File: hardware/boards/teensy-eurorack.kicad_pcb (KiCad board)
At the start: 2 copper layers, 118.1 x 224.8 mm, 166 parts, among them J1 Conn_01x08, J10 AudioJack3_SwitchTR, J27 Conn_01x02, J28 Conn_02x08_Odd_Even, J4 AudioJack3_SwitchTR, J5 AudioJack3_SwitchTR, J57 WURTH_ELECTRONICS_61400413321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, J58 USB-A-S-X-X-VT, J6 AudioJack3_SwitchTR, J7 AudioJack3_SwitchTR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

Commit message: silkscreen
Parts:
- U5: value MCP1700-2502E_SOT23 -> MCP1700-2502E
- moved C4 20.0 mm to (206.8, -2.79)
- moved C8 17.9 mm to (214.9, -14.2), turned to 270 degrees
- moved C9 13.6 mm to (212.6, -14.2), turned to 270 degrees
- moved C17 13.5 mm to (219.2, -22.6)
- moved C3 12.6 mm to (215.4, -2.79)
- moved C10 9.31 mm to (210.3, -14.2), turned to 270 degrees
- moved C11 8.86 mm to (217.2, -14.2), turned to 270 degrees
- moved C16 7.90 mm to (219.5, -19.1)
- moved C6 7.60 mm to (209.0, -34.8), turned to 90 degrees
- moved R3 6.02 mm to (195.6, -12.1)
- moved R4 5.50 mm to (195.6, -15.6)
- moved C18 5.35 mm to (208.0, -14.2), turned to 270 degrees
- moved C14 4.49 mm to (205.7, -14.2), turned to 90 degrees
- moved C30 3.99 mm to (184.9, -122.9)
- moved C7 3.32 mm to (206.8, -34.8), turned to 90 degrees
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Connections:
- JB3 pad 2: /ES2 -> /P2
- JB3 pad 3: /ES1 -> /P1
- JB3 pad 4: /P4 -> /E3B
- JB3 pad 5: /P3 -> /E3A
- JB3 pad 6: /P2 -> /ES3
- JB3 pad 7: /P1 -> GND
- JB3 pad 8: GND -> /P3
- JB4 pad 2: /E3B -> /P4
- JB4 pad 3: /E3A -> /ES1
- JB4 pad 4: /E2B -> /E1B
- JB4 pad 5: /E2A -> /E1A
- JB4 pad 6: /E1B -> /ES2
- JB4 pad 7: /E1A -> /E2B
- JB4 pad 8: /ES3 -> /E2A
- JM3 pad 2: /ES2 -> /P2
- JM3 pad 3: /ES1 -> /P1
- JM3 pad 4: /P4 -> /E3B
- JM3 pad 5: /P3 -> /E3A
- JM3 pad 6: /P2 -> /ES3
- JM3 pad 7: /P1 -> GND
- JM3 pad 8: GND -> /P3
- JM4 pad 2: /E3B -> /P4
- JM4 pad 3: /E3A -> /ES1
- JM4 pad 4: /E2B -> /E1B
- JM4 pad 5: /E2A -> /E1A
- JM4 pad 6: /E1B -> /ES2
- JM4 pad 7: /E1A -> /E2B
- JM4 pad 8: /ES3 -> /E2A

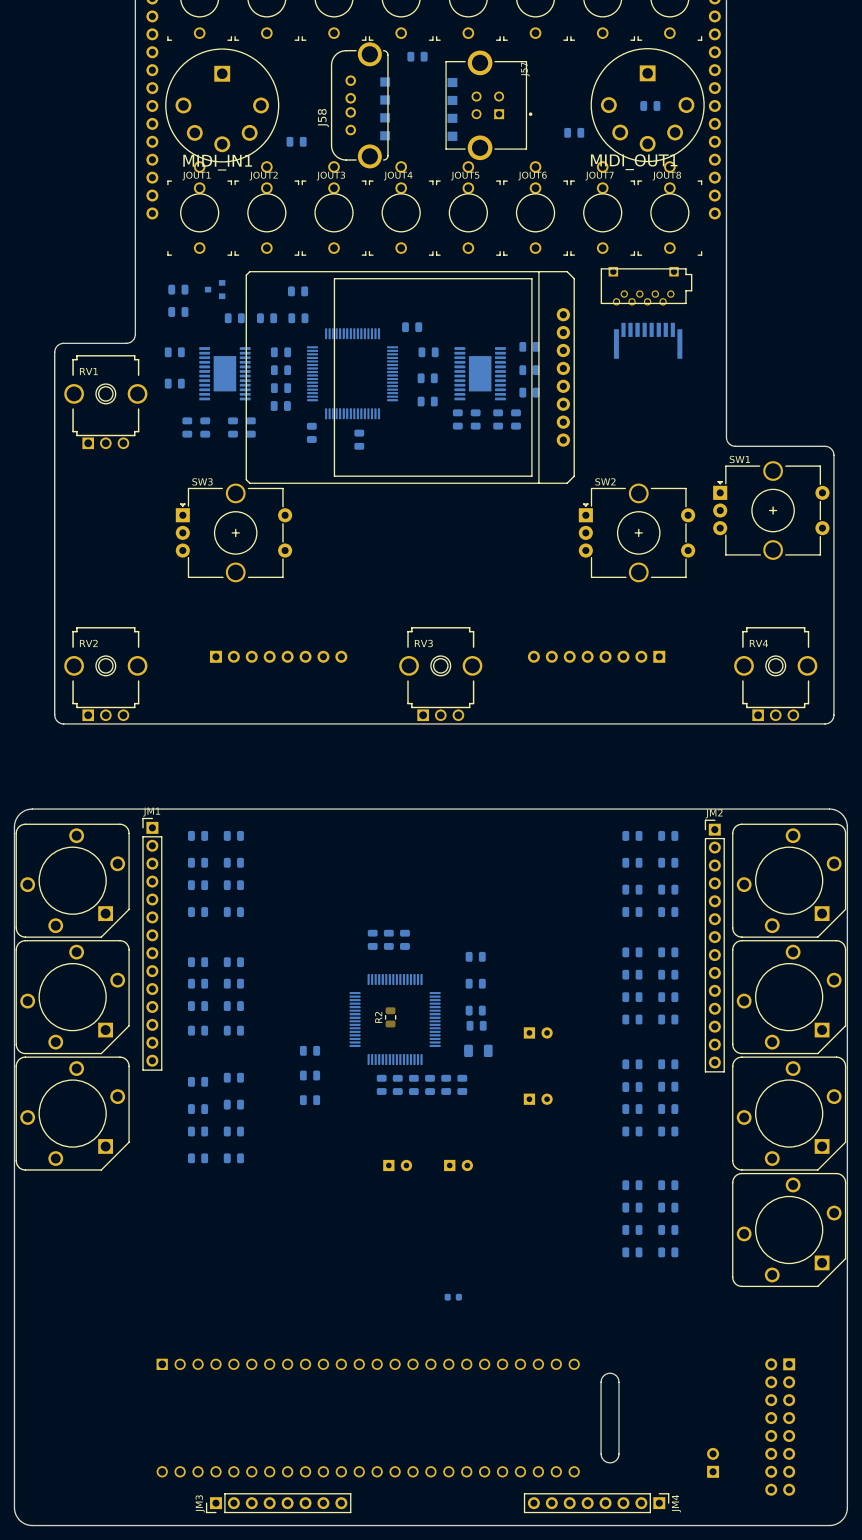
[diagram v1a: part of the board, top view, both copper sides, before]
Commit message: silkscreen, corrections
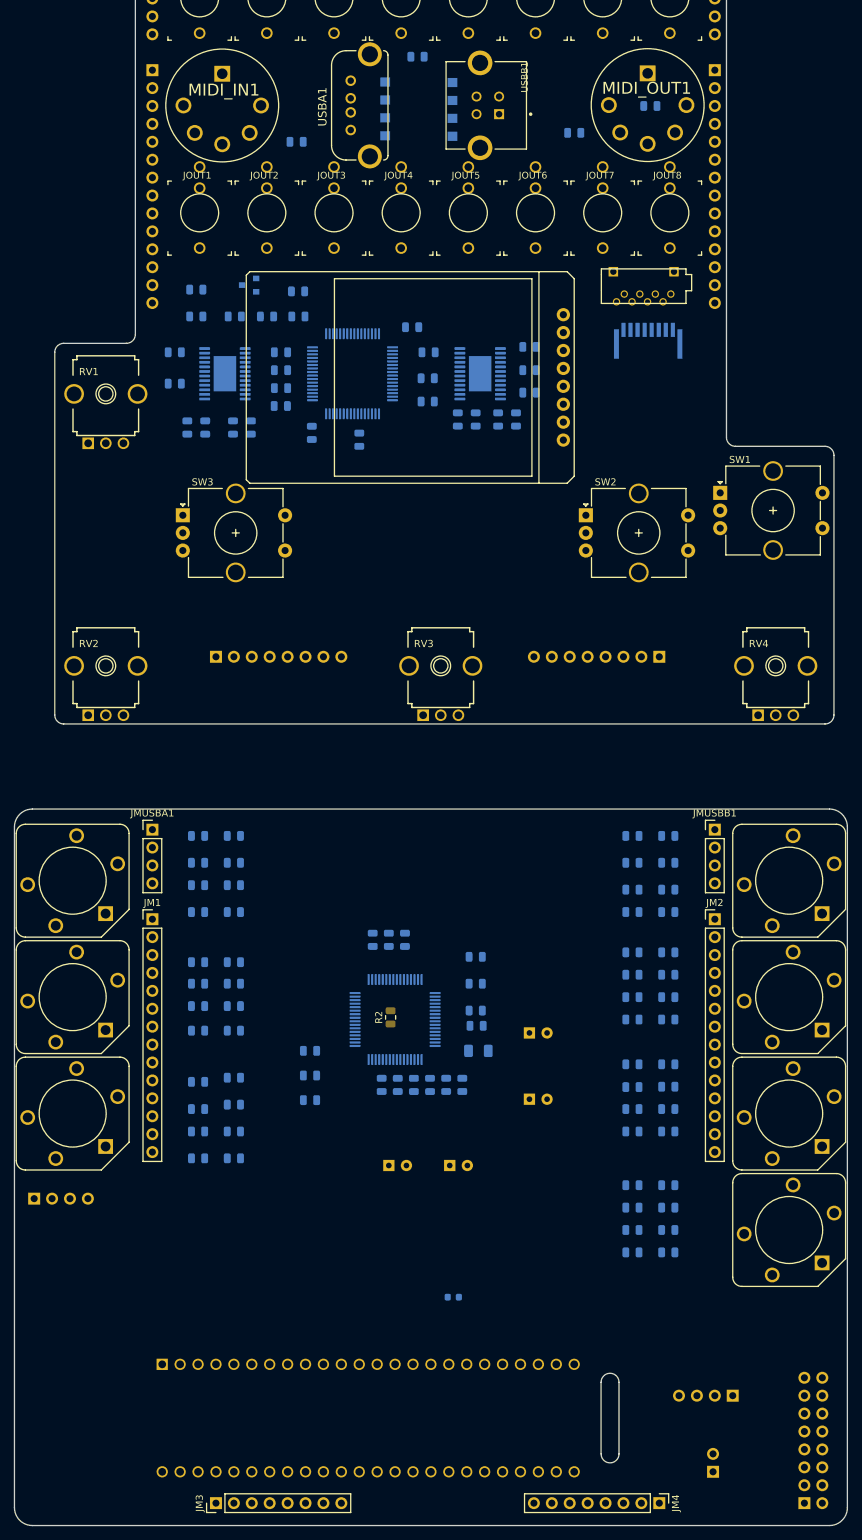
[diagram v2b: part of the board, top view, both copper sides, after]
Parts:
- added JBUSBA1: Conn_01x04, Connector_PinSocket_2.54mm:PinSocket_1x04_P2.54mm_Vertical, B.Cu at (173.2, -170.8)
- added JBUSBB1: Conn_01x04, Connector_PinSocket_2.54mm:PinSocket_1x04_P2.54mm_Vertical, B.Cu at (253.0, -170.8)
- added JMUSBA1: Conn_01x04, Connector_PinHeader_2.54mm:PinHeader_1x04_P2.54mm_Vertical, F.Cu at (173.2, -50.4)
- added JMUSBB1: Conn_01x04, Connector_PinHeader_2.54mm:PinHeader_1x04_P2.54mm_Vertical, F.Cu at (253.0, -50.4)
- added JUSBA1: Conn_01x04, Connector_PinHeader_2.54mm:PinHeader_1x04_P2.54mm_Vertical, B.Cu at (156.5, 1.91)
- added JUSBB1: Conn_01x04, Connector_PinHeader_2.54mm:PinHeader_1x04_P2.54mm_Vertical, B.Cu at (255.5, 29.8)
- C12: value 4.7uF -> 4.7u
- C14: value 22uF -> 22u
- C16: value 100uF -> 100u
- C27, C29, C33, C34, C37: value 10uF -> 10u
- USBB1: renamed from J57; value WURTH_ELECTRONICS_61400413321WURTH_ELECTRONICS_61400413321_0_0 -> 61400413321
- moved J28 19.8 mm to (265.7, 45.1), turned to 0 degrees
- moved JM1 13.0 mm to (173.2, -37.7)
- moved JM2 12.7 mm to (253.0, -37.7)
- moved JB1 12.7 mm to (173.2, -158.1)
- moved JB2 12.7 mm to (253.0, -158.1)
- moved U5 4.87 mm to (186.9, -127.6)
- moved C28 2.62 mm to (179.5, -123.2)
- moved C27 2.54 mm to (179.5, -127.0)
- moved C29 0.25 mm to (189.5, -123.2)
- moved C30 0.25 mm to (184.9, -123.2)
- moved C40 0.25 mm to (193.9, -123.2)
- renumbered J58 to USBA1
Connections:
- USBA1 pad 1: (no net) -> Net-(JBUSBA1-Pad4)
- USBA1 pad 2: (no net) -> Net-(JBUSBA1-Pad3)
- USBA1 pad 3: (no net) -> Net-(JBUSBA1-Pad2)
- USBA1 pad 4: (no net) -> Net-(JBUSBA1-Pad1)
- USBB1 pad 1: (no net) -> Net-(JBUSBB1-Pad4)
- USBB1 pad 2: (no net) -> Net-(JBUSBB1-Pad3)
- USBB1 pad 3: (no net) -> Net-(JBUSBB1-Pad2)
- USBB1 pad 4: (no net) -> GND
- USBB1 pad 5: (no net) -> Net-(USBB1-Pad5)
- USBB1 pad 6: (no net) -> Net-(USBB1-Pad6)

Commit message: split into two boards
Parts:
- removed C19, C20, C21, C22, C27, C29, C33, C34, C37, C42: 10u, Capacitor_SMD:C_0805_2012Metric
- removed C23, C24, C25, C26, C28, C30, C31, C32, C35, C36, C38, C39, C40, C41: 0.1u, Capacitor_SMD:C_0805_2012Metric
- removed C43, C44: 1u, Capacitor_SMD:C_0805_2012Metric
- removed D1: D, Diode_SMD:D_0805_2012Metric
- removed FPC_SD1: 1734592-8, footprints:HFW8R-1STE1LF
- removed J1: Conn_01x08, footprints:ST7735
- removed JB1, JB2: Conn_01x14, Connector_PinSocket_2.54mm:PinSocket_1x14_P2.54mm_Vertical
- removed JB3, JB4: Conn_01x08, Connector_PinSocket_2.54mm:PinSocket_1x08_P2.54mm_Vertical
- removed JBUSBA1, JBUSBB1: Conn_01x04, Connector_PinSocket_2.54mm:PinSocket_1x04_P2.54mm_Vertical
- removed JIN1, JIN2, JIN3, JIN4, JIN5, JIN6, JIN7, JIN8, JOUT1, JOUT2, JOUT3, JOUT4, JOUT5, JOUT6, JOUT7, JOUT8: AudioJack2_SwitchT, footprints:WQP-PJ301M-12_JACK
- removed MIDI_IN1, MIDI_OUT1: DIN-5, footprints:OG-MIDI_SD-50BV
- removed R36, R37, R38: 220, Resistor_SMD:R_0805_2012Metric
- removed R5, R6, R7: 4.7k, Resistor_SMD:R_0805_2012Metric
- removed RV1, RV2, RV3, RV4: R_POT, footprints:9MM_SNAP-IN_POT
- removed SDCARD1: YAMAICHI_SD_CARD, footprints:YAMAICHI_MICROSD_VERTICAL
- removed SW1, SW2, SW3: Rotary_Encoder_Switch, Rotary_Encoder:RotaryEncoder_Alps_EC12E-Switch_Vertical_H20mm_CircularMountingHoles
- removed U2, U3: AD5754BREZ, Package_SO:HTSSOP-24-1EP_4.4x7.8mm_P0.65mm_EP3.2x5mm
- removed U5: MCP1700-2502E, Package_TO_SOT_SMD:SOT-23
- removed U6: AD7606BSTZ, Package_QFP:LQFP-64_10x10mm_P0.5mm
- removed U7: 6N138, footprints:6N138S
- removed USBA1: USB-A-S-X-X-VT, footprints:USB-A-S-X-X-VT
- removed USBB1: 61400413321, footprints:WURTH_ELECTRONICS_61400413321_0
- moved FB1 41.1 mm to (248.7, 40.6)
- moved C15 22.8 mm to (207.1, -13.0), turned to 180 degrees
- moved C17 18.7 mm to (208.9, -6.99), turned to 270 degrees
- moved C16 18.7 mm to (205.7, -6.35), turned to 270 degrees
- moved C5 15.3 mm to (195.7, -22.2), turned to 180 degrees
- moved C18 11.7 mm to (219.7, -14.2)
- moved C64 3.94 mm to (184.8, -7.49)
- moved C12 3.68 mm to (219.1, -24.9)
- moved C63 3.43 mm to (184.8, -11.0)
- moved C3 3.17 mm to (215.4, 0.38)
- moved C4 3.17 mm to (206.8, 0.38)
- moved C13 2.54 mm to (219.1, -22.2)
- moved C14 1.73 mm to (207.1, -15.2), turned to 180 degrees
- moved C61 0.63 mm to (184.8, -14.6)
- moved R24 0.25 mm to (179.7, -11.0)
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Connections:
- U1 pad 15: Net-(U1-Pad15) -> GND
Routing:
- net /ADC_MISO: track 0.00 -> 319.7 mm
- net +3V3: track 0.00 -> 255.5 mm, vias 0 -> 7
- net +12V: track 0.00 -> 248.5 mm, vias 0 -> 3
- net -12V: track 0.00 -> 243.0 mm
- net +5V: track 0.00 -> 152.2 mm
- net /SDA: track 0.00 -> 134.5 mm, vias 0 -> 3
- net /AGND: track 0.00 -> 133.9 mm, vias 0 -> 42
- net /MIDI_RX: track 0.00 -> 123.7 mm, vias 0 -> 1
- net Net-(C10-Pad1): track 0.00 -> 107.7 mm, vias 0 -> 2
- net /LRCLK: track 0.00 -> 100.2 mm
- net Net-(JMUSBB1-Pad4): track 0.00 -> 96.6 mm
- net /BCLK: track 0.00 -> 96.0 mm, vias 0 -> 2
- net Net-(JMUSBB1-Pad2): track 0.00 -> 92.7 mm
- net Net-(JMUSBB1-Pad3): track 0.00 -> 91.8 mm
- net /TFT_CS: track 0.00 -> 91.3 mm, vias 0 -> 2
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- added copper zone on F.Cu, net /AGND
- added copper zone on B.Cu, net GND
- added copper zone on F.Cu, net GND
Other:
- board size 118.1 x 224.8 mm -> 118.1 x 101.6 mm
- rule trace_min: 0.2 -> 0.1524
- rule via_min_drill: 0.3 -> 0.1143
- rule via_min_size: 0.4 -> 0.2286

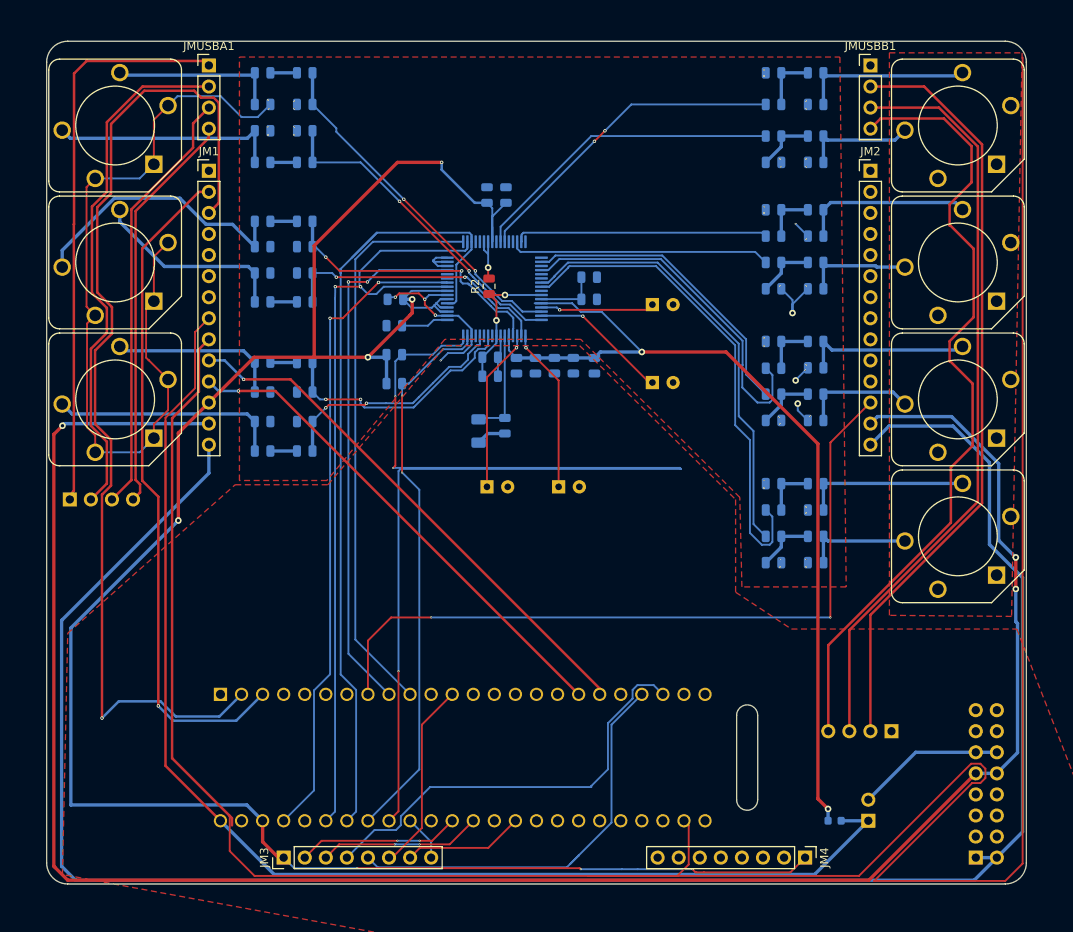
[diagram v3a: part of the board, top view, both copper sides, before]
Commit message: mainboard passes drc
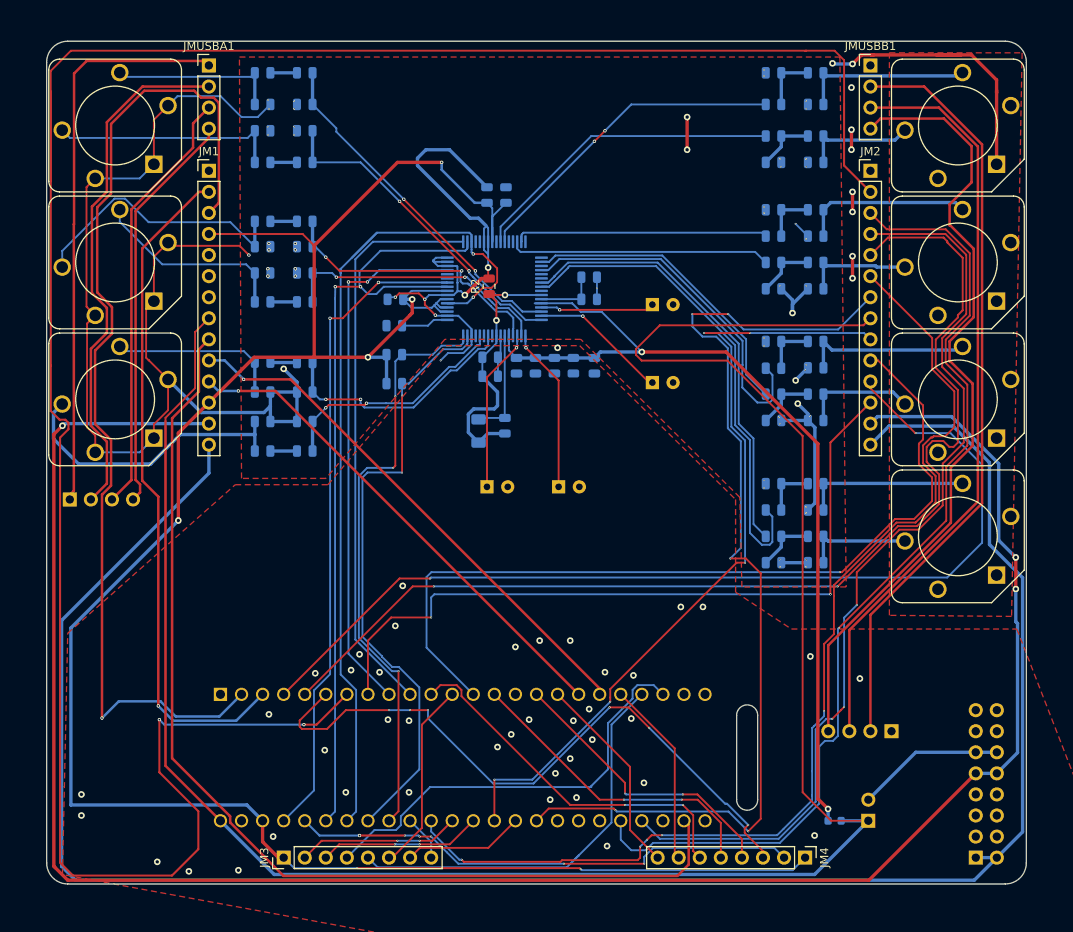
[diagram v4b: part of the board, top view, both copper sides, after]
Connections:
- J28 pad 3: Net-(J28-Pad3) -> GND
- J28 pad 4: Net-(J28-Pad4) -> GND
- J28 pad 5: Net-(J28-Pad3) -> GND
- J28 pad 6: Net-(J28-Pad4) -> GND
- J28 pad 7: Net-(J28-Pad3) -> GND
- J28 pad 8: Net-(J28-Pad4) -> GND
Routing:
- net /ADC_CONVST: track 0.00 -> 283.1 mm, vias 0 -> 2
- net /ADC_MISO: track 319.7 -> 127.0 mm
- net /ADC_BUSY: track 0.00 -> 135.9 mm, vias 0 -> 2
- net /DAC_SYNC: track 0.00 -> 130.6 mm, vias 0 -> 5
- net /DAC_SDOUT: track 0.00 -> 120.6 mm, vias 0 -> 5
- net /ADC_SCK: track 0.00 -> 119.6 mm, vias 0 -> 1
- net /TFT_DC: track 0.00 -> 119.3 mm, vias 0 -> 2
- net /ADC_CS: track 0.00 -> 113.7 mm, vias 0 -> 3
- net /AGND: track 133.9 -> 245.5 mm, vias 42 -> 55
- net +5V: track 152.2 -> 259.2 mm
- net /TFT_MOSI: track 0.00 -> 102.2 mm, vias 0 -> 1
- net /TFT_SCK: track 0.00 -> 98.0 mm, vias 0 -> 6
- net /ES1: track 0.00 -> 79.3 mm, vias 0 -> 6
- net /SDA: track 134.5 -> 71.9 mm
- net /P4: track 0.00 -> 61.7 mm, vias 0 -> 6
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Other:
- net class Default: clearance 0.2 -> 0.1524; trace_width 0.25 -> 0.2286
- rule trace_clearance: 0.2 -> 0.1524

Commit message: routing improv
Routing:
- net GND: track 97.0 -> 122.6 mm, vias 57 -> 68
- net /AudioOut.sch/RIGHT: track 39.1 -> 42.8 mm, vias 2 -> 0
- net /SCL: track 73.8 -> 72.1 mm
- net /MCLK: track 78.8 -> 79.7 mm
- net /SDA: track 71.9 -> 71.1 mm
- net /BCLK: track 96.0 -> 96.7 mm
- net /TDM_OUT: track 69.1 -> 69.6 mm
- net /ADC_BUSY: track 135.9 -> 136.4 mm
- net /TFT_CS: track 91.1 -> 90.8 mm, vias 3 -> 2
- net /AGND: vias 55 -> 58

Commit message: silkscreen improvments, gerbers, drc'ed
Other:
- board text added: "D+"
- board text added: "D-"
- board text added: "USB A"
- board text added: "USB B"
- board text added: "VCC"
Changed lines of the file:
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@@
   (general
     (thickness 1.6)
-    (drawings 12)
+    (drawings 20)
     (tracks 1430)
     (zones 0)
@@
     (34 B.Paste user hide)
     (35 F.Paste user hide)
-    (36 B.SilkS user hide)
-    (37 F.SilkS user hide)
+    (36 B.SilkS user)
+    (37 F.SilkS user)
     (38 B.Mask user hide)
     (39 F.Mask user hide)
@@
       (outputformat 1)
       (mirror false)
-      (drillshape 1)
+      (drillshape 0)
       (scaleselection 1)
-      (outputdirectory ""))
+      (outputdirectory "gerbers-mainboard"))
   )
   (net 0 "")
@@
     )
   )
+  (gr_text VCC (at 164.211 5.842 90) (layer B.SilkS)
+    (effects (font (size 1.5 1.5) (thickness 0.3)) (justify mirror))
+  )
+  (gr_text D- (at 161.671 5.377715 90) (layer B.SilkS)
+    (effects (font (size 1.5 1.5) (thickness 0.3)) (justify mirror))
+  )
+  (gr_text D+ (at 159.131 5.377715 90) (layer B.SilkS)
+    (effects (font (size 1.5 1.5) (thickness 0.3)) (justify mirror))
+  )
+  (gr_text "USB A" (at 161.798 -0.635) (layer B.SilkS)
+    (effects (font (size 1.5 1.5) (thickness 0.3)) (justify mirror))
+  )
+  (gr_text "USB B" (at 250.317 27.051) (layer B.SilkS)
+    (effects (font (size 1.5 1.5) (thickness 0.3)) (justify mirror))
+  )
+  (gr_text VCC (at 248.031 33.738286 270) (layer B.SilkS)
+    (effects (font (size 1.5 1.5) (thickness 0.3)) (justify mirror))
+  )
+  (gr_text D- (at 250.444 33.274 270) (layer B.SilkS)
+    (effects (font (size 1.5 1.5) (thickness 0.3)) (justify mirror))
+  )
+  (gr_text D+ (at 252.984 33.274 270) (layer B.SilkS)
+    (effects (font (size 1.5 1.5) (thickness 0.3)) (justify mirror))
+  )
   (gr_line (start 153.67 45.72) (end 153.67 -50.8) (layer Edge.Cuts) (width 0.1))
   (gr_line (start 156.21 -53.34) (end 269.24 -53.34) (layer Edge.Cuts) (width 0.1))
@@
   (gr_arc (start 269.24 45.72) (end 269.24 48.26) (angle -90) (layer Edge.Cuts) (width 0.1))
   (gr_arc (start 156.21 45.72) (end 153.67 45.72) (angle -90) (layer Edge.Cuts) (width 0.1))
-  (via (at 180.34 -25.019) (size 0.4064) (drill 0.2032) (layers F.Cu B.Cu) (net 8))
-  (via (at 180.34 -25.908) (size 0.4064) (drill 0.2032) (layers F.Cu B.Cu) (net 8))
-  (via (at 183.642 -25.019) (size 0.4064) (drill 0.2032) (layers F.Cu B.Cu) (net 8))
-  (via (at 183.642 -25.908) (size 0.4064) (drill 0.2032) (layers F.Cu B.Cu) (net 8))
-  (via (at 180.467 -28.194) (size 0.4064) (drill 0.2032) (layers F.Cu B.Cu) (net 8))
-  (via (at 183.642 -28.194) (size 0.4064) (drill 0.2032) (layers F.Cu B.Cu) (net 8))
-  (via (at 183.642 -28.956) (size 0.4064) (drill 0.2032) (layers F.Cu B.Cu) (net 8))
-  (via (at 180.467 -28.956) (size 0.4064) (drill 0.2032) (layers F.Cu B.Cu) (net 8))
   (segment (start 206.395 -29.17) (end 206.395 -28.174) (width 0.2286) (layer B.Cu) (net 1))
   (segment (start 206.895 -27.674) (end 206.895 -26.047) (width 0.2286) (layer B.Cu) (net 1))
@@
   (segment (start 220.589499 -20.710501) (end 225.425 -15.875) (width 0.2286) (layer B.Cu) (net 7))
   (segment (start 213.32 -21.745) (end 217.0301 -21.745) (width 0.2286) (layer B.Cu) (net 7))
+  (via (at 180.34 -25.019) (size 0.4064) (drill 0.2032) (layers F.Cu B.Cu) (net 8))
+  (via (at 180.34 -25.908) (size 0.4064) (drill 0.2032) (layers F.Cu B.Cu) (net 8))
+  (via (at 183.642 -25.019) (size 0.4064) (drill 0.2032) (layers F.Cu B.Cu) (net 8))
+  (via (at 183.642 -25.908) (size 0.4064) (drill 0.2032) (layers F.Cu B.Cu) (net 8))
+  (via (at 180.467 -28.194) (size 0.4064) (drill 0.2032) (layers F.Cu B.Cu) (net 8))
+  (via (at 183.642 -28.194) (size 0.4064) (drill 0.2032) (layers F.Cu B.Cu) (net 8))
+  (via (at 183.642 -28.956) (size 0.4064) (drill 0.2032) (layers F.Cu B.Cu) (net 8))
+  (via (at 180.467 -28.956) (size 0.4064) (drill 0.2032) (layers F.Cu B.Cu) (net 8))
   (via (at 180.34 -46.228) (size 0.2286) (drill 0.1143) (layers F.Cu B.Cu) (net 8))
   (via (at 180.467 -45.212) (size 0.2286) (drill 0.1143) (layers F.Cu B.Cu) (net 8))
